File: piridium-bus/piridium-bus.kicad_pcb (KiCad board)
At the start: 4 copper layers, 90.2 x 95.9 mm, 129 parts, among them J1 EPS, J2 MODEM UART, J3 INHIBITS, J4 ANT, J5 PAYLOAD, J6 IN1, J7 IN2, J8 IN1, J9 IN2, Q1 DMP3015LSSQ, Q2 Si4186DY, Q3 DMP3015LSSQ, Q4 Si4186DY, Q5 DMP3015LSSQ, Q6 DMP3015LSSQ, Q7 2N7002, Q8 DMP3015LSSQ, U1 LM1117-3.3, U10 INA180A3, U11 LT3652EMSE, U12 INA180A3, U2 TPS54394RSAR, U3 MAX6369, U4 74HC126, U5 INA180A3, U6 DS3232M, U7 INA180A3, U8 MCP3208, U9 LT3652EMSE

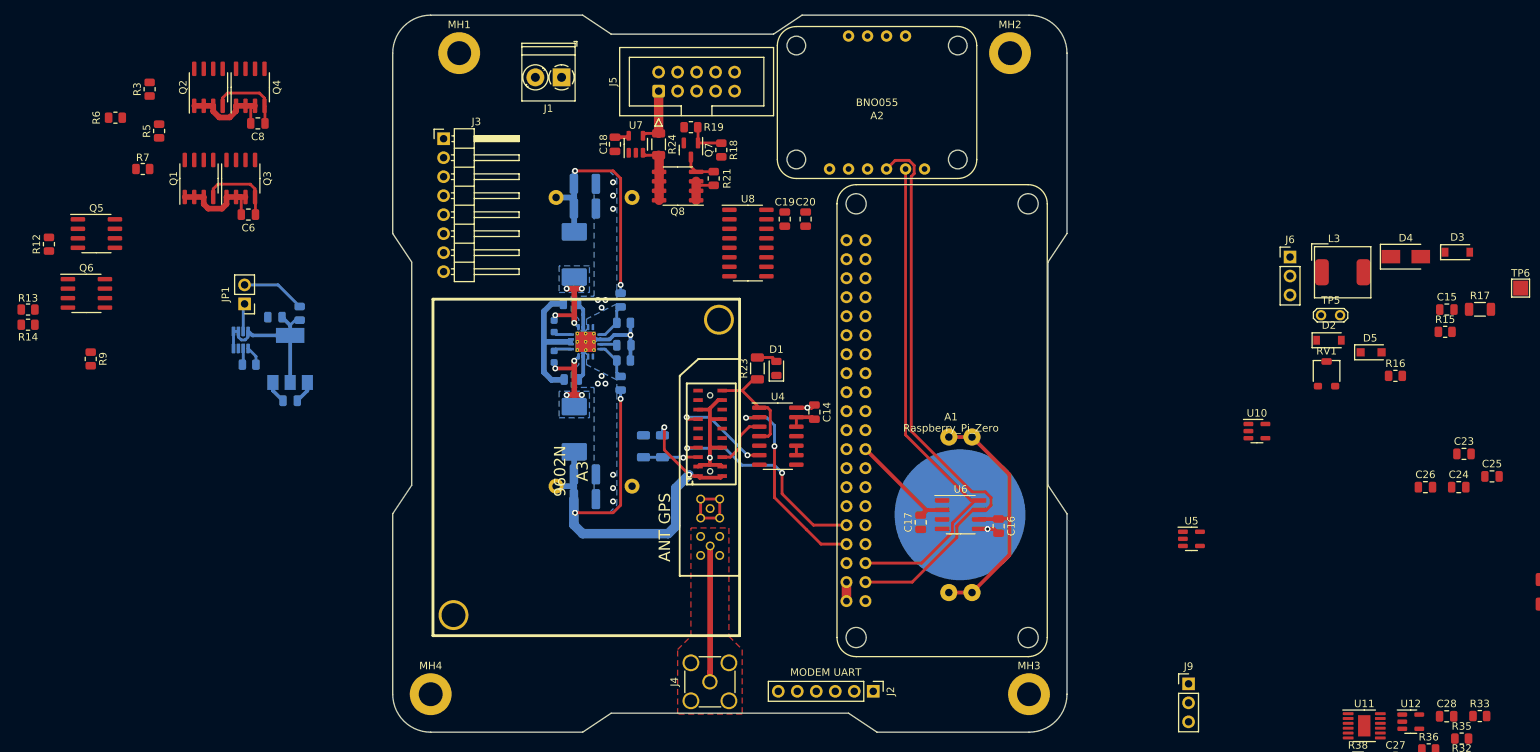
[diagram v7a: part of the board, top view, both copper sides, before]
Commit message: route inhibits and some other power path stuff
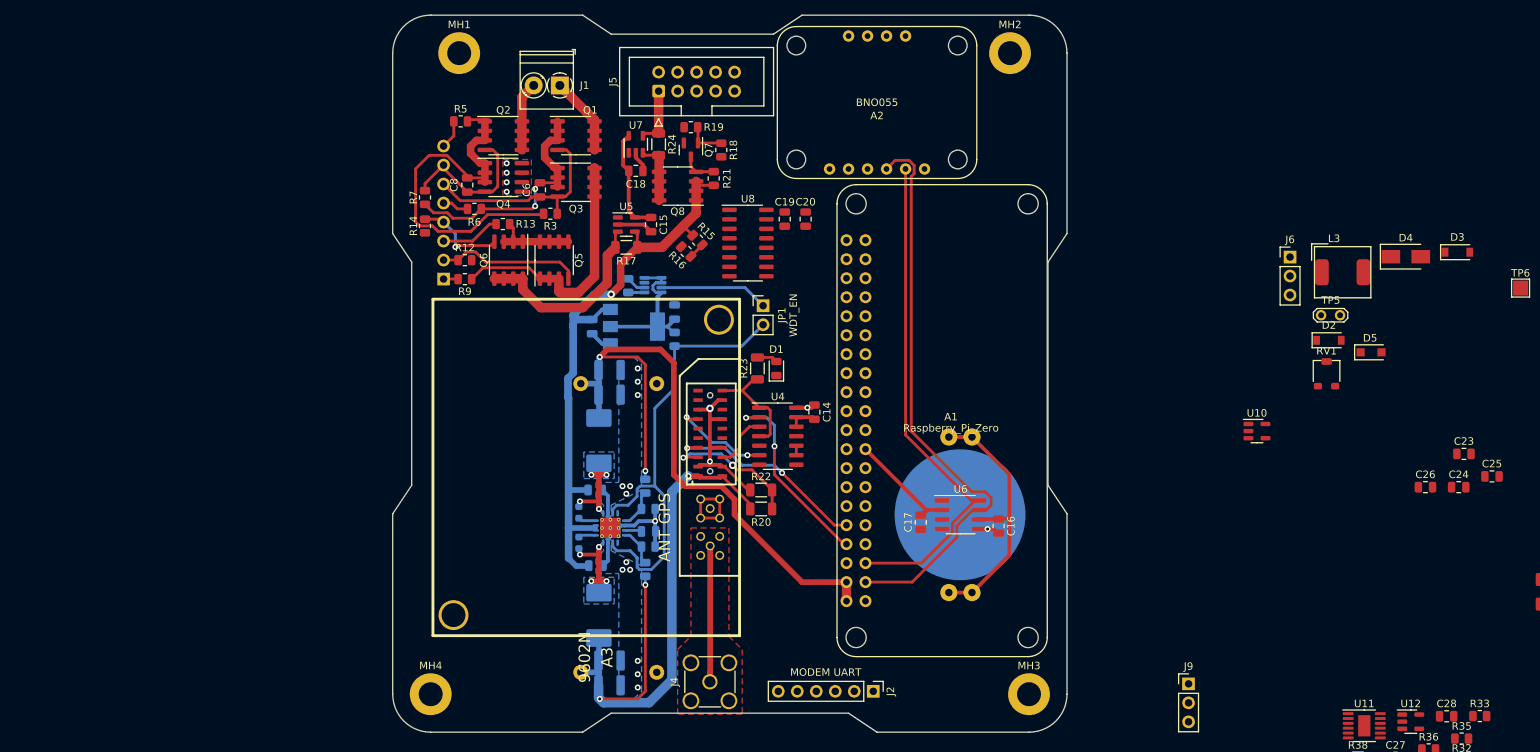
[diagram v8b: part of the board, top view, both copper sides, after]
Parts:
- J3: moved to B.Cu
- R20, R22: moved to F.Cu
- moved R17 114.5 mm to (132.8, 81.9), turned to 180 degrees
- moved C15 107.0 mm to (136.1, 78.8), turned to -90 degrees
- moved R15 100.7 mm to (142.4, 80.9), turned to -45 degrees
- moved R16 96.3 mm to (140.8, 82.4), turned to 135 degrees
- moved U5 86.5 mm to (132.8, 78.8)
- moved JP1 69.3 mm to (151.1, 89.7), turned to 0 degrees
- moved R13 64.5 mm to (116.3, 78.7)
- moved Q5 61.3 mm to (123.2, 83.6), turned to 90 degrees
- moved Q6 56.6 mm to (117.1, 83.6), turned to -90 degrees
- moved R3 56.1 mm to (122.7, 77.4), turned to 180 degrees
- moved R12 55.7 mm to (111.3, 83.6), turned to 0 degrees
- moved U3 55.6 mm to (136.4, 86.9), turned to 0 degrees
- moved R14 54.7 mm to (105.9, 79.0), turned to -90 degrees
- moved C5 53.4 mm to (139.3, 90.5), turned to 90 degrees
- moved R4 51.8 mm to (133.1, 87.0), turned to 90 degrees
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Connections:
- R15 pad 1: Net-(Q6-Pad5) -> +BATT
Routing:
- net +BATT: track 25.8 -> 82.5 mm, vias 0 -> 1
- net +5V: track 35.0 -> 91.3 mm
- net /EN: track 8.56 -> 60.9 mm
- net /CHARGE_OUT: track 0.00 -> 38.6 mm
- net Net-(C8-Pad2): track 12.7 -> 50.3 mm
- net Net-(Q6-Pad5): track 0.00 -> 26.4 mm
- net Net-(C6-Pad1): track 12.9 -> 32.9 mm, vias 0 -> 2
- net /B1L: track 0.00 -> 19.3 mm
- net /A1L: track 10.6 -> 27.7 mm
- net GND: track 50.3 -> 63.6 mm, vias 15 -> 20
- net +5VP: track 71.7 -> 84.2 mm, vias 4 -> 3
- net /B2L: track 0.00 -> 12.1 mm, vias 0 -> 1
- net +3.3V: track 20.0 -> 32.2 mm
- net S_MODEM_ON_OFF: track 7.37 -> 18.7 mm, vias 1 -> 2
- net Net-(Q5-Pad5): track 0.00 -> 11.2 mm
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- added copper zone on F.Cu, net GND
- removed copper zone on In1.Cu, net +3.3V
- removed copper zone on In2.Cu, net GND
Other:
- copper layers 4 -> 2
